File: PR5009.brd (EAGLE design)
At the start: 70 x 70 mm, 47 parts

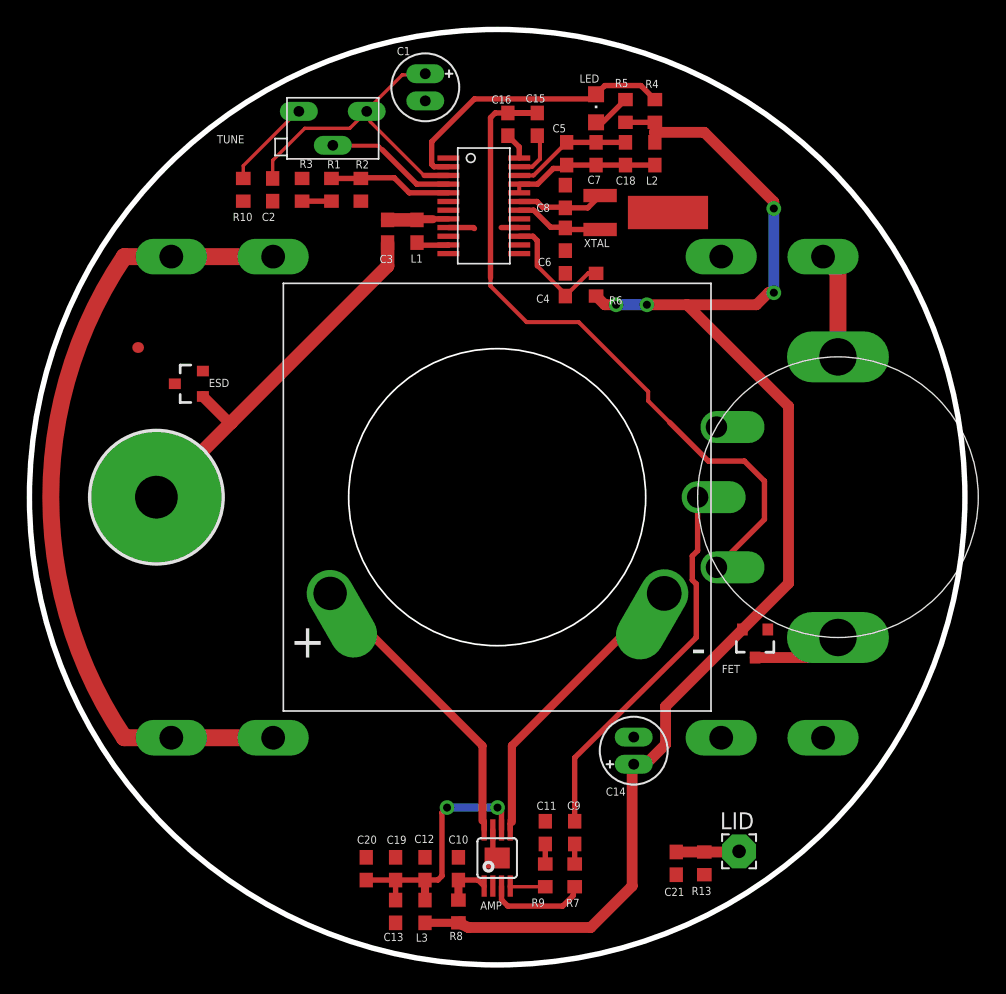
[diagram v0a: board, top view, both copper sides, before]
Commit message: Updates and Fixes
Small changes, clearing Osh Park design rules
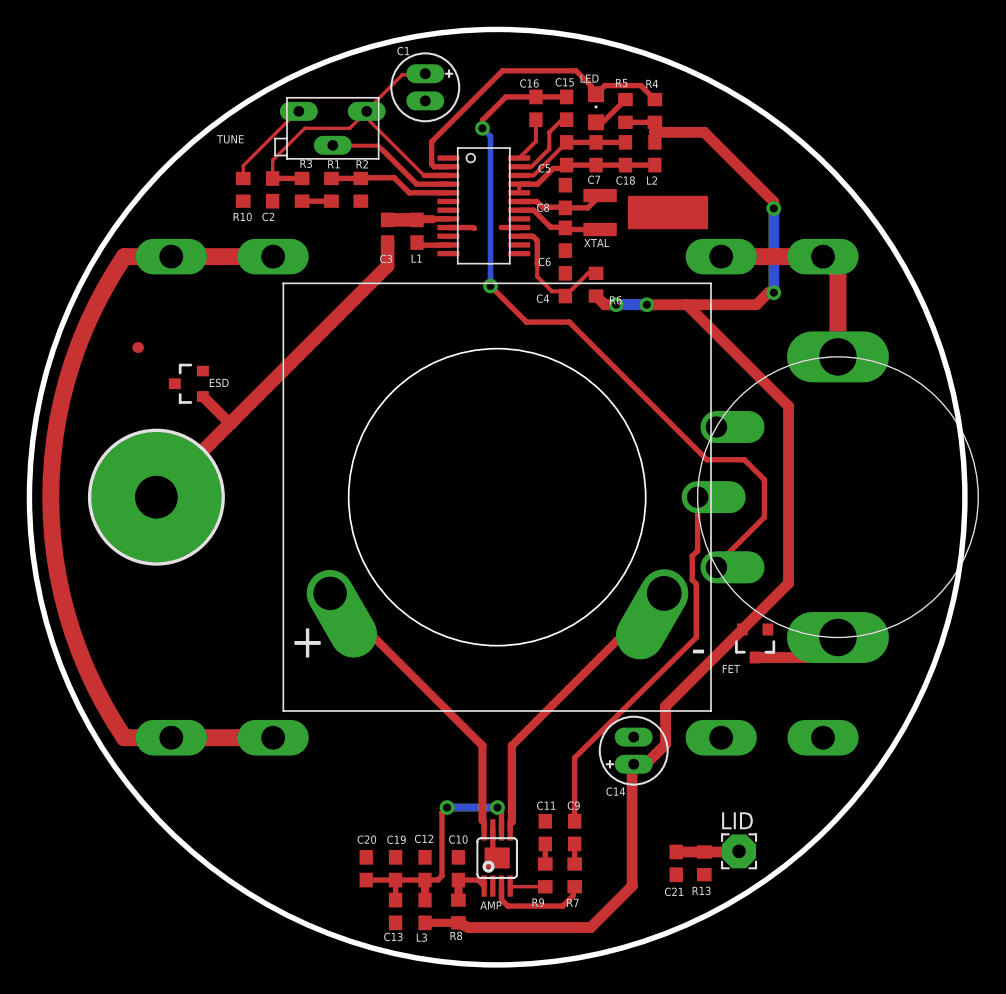
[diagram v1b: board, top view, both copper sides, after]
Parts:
- moved C15 2.51 mm to (40.2, 64.1)
- moved C16 2.42 mm to (37.9, 64.1)
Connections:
- removed net N$35: R3.2
- net N$22: now also R3.2
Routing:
- net N$21: track 7.96 -> 15.6 mm
- net N$9: track 21.9 -> 24.2 mm
- net N$31: track 3.76 -> 6.01 mm
- net N$22: track 23.9 -> 26.1 mm
- net N$33: track 2.03 -> 3.39 mm
- net N$5: track 53.3 -> 54.2 mm, vias 0 -> 2
- net N$8: track 9.51 -> 10.2 mm

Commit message: Single Layer Update
Updated Layout
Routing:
- net VCC: vias 4 -> 2
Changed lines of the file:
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@@
 <layer number="20" name="Dimension" color="15" fill="1" visible="yes" active="yes"/>
 <layer number="21" name="tPlace" color="7" fill="1" visible="yes" active="yes"/>
-<layer number="22" name="bPlace" color="7" fill="1" visible="no" active="yes"/>
+<layer number="22" name="bPlace" color="7" fill="1" visible="yes" active="yes"/>
 <layer number="23" name="tOrigins" color="15" fill="1" visible="yes" active="yes"/>
 <layer number="24" name="bOrigins" color="15" fill="1" visible="no" active="yes"/>
@@
 <circle x="35" y="35" radius="12.5" width="0.4064" layer="42"/>
 <text x="28.5254" y="52.5508" size="0.6096" layer="25" ratio="16">L1</text>
-<text x="14.0286" y="61.4778" size="0.6096" layer="25" ratio="16">TUNE</text>
+<text x="16.1586" y="62.7778" size="0.6096" layer="25" ratio="16">TUNE</text>
 <rectangle x1="12.03" y1="8.67" x2="12.21" y2="8.73" layer="214"/>
 <rectangle x1="11.67" y1="9.75" x2="11.85" y2="9.81" layer="211"/>
@@
 </element>
 <element name="R6" library="resistor" package="R0603" value="100K" x="42.4" y="50.9" smashed="yes" rot="R270">
-<attribute name="NAME" x="43.37" y="49.425" size="0.6096" layer="25" ratio="16"/>
+<attribute name="NAME" x="44.02" y="51.405" size="0.6096" layer="25" ratio="16"/>
 <attribute name="VALUE" x="40.368" y="51.789" size="0.8128" layer="27" rot="R270"/>
 </element>
@@
 </element>
 <element name="C1" library="CPOL-US-LongPads " package="E2-5" value="47uf" x="29.62" y="65.67" smashed="yes" rot="R270">
-<attribute name="NAME" x="27.493" y="68.0732" size="0.6096" layer="25" ratio="16"/>
+<attribute name="NAME" x="26.323" y="67.2332" size="0.6096" layer="25" ratio="16"/>
 <attribute name="VALUE" x="27.461" y="63.13" size="1.27" layer="27" ratio="10" rot="R270"/>
 </element>
@@
 <wire x1="32.85" y1="2.8" x2="32.1" y2="3.15" width="0.8128" layer="1"/>
 <wire x1="56.8" y1="41.8" x2="49.2" y2="49.4" width="0.8128" layer="1"/>
-<wire x1="49.2" y1="49.4" x2="46.2" y2="49.4" width="0.8128" layer="1"/>
-<via x="46.2" y="49.4" extent="1-16" drill="0.6"/>
-<wire x1="46.2" y1="49.4" x2="43.9" y2="49.4" width="0.8128" layer="16"/>
-<via x="43.9" y="49.4" extent="1-16" drill="0.6"/>
-<wire x1="43.9" y1="49.4" x2="43.05" y2="49.4" width="0.8128" layer="1"/>
-<wire x1="43.05" y1="49.4" x2="42.4" y2="50.05" width="0.8128" layer="1"/>
 <wire x1="49.2" y1="49.4" x2="54.4" y2="49.4" width="0.8128" layer="1"/>
 <via x="55.7" y="50.3" extent="1-16" drill="0.6"/>
@@
 <wire x1="45.1" y1="5.9" x2="45.1" y2="14.9004" width="0.8128" layer="1"/>
 <wire x1="45.1" y1="14.9004" x2="45.2168" y2="15.0172" width="0.8128" layer="1"/>
+<wire x1="42.4" y1="50.05" x2="43.05" y2="49.4" width="0.8128" layer="1"/>
+<wire x1="49.2" y1="49.4" x2="43.05" y2="49.4" width="0.8128" layer="1"/>
 </signal>
 <signal name="N$1">
